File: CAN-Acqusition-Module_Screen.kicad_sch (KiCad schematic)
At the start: 5 parts, among them U9 ERC13232FN-1

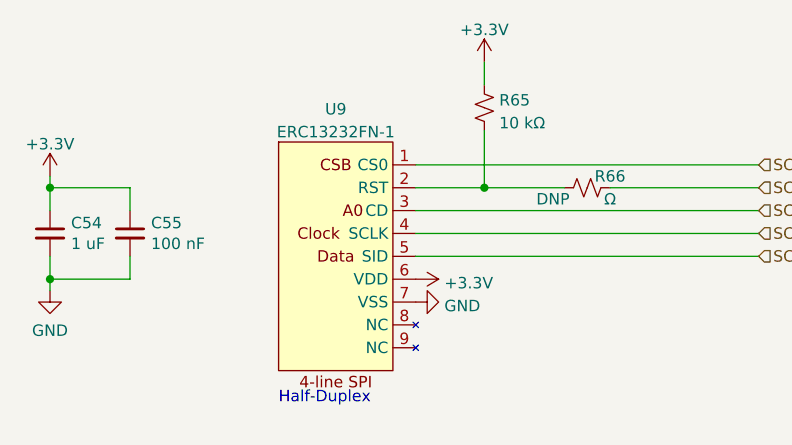
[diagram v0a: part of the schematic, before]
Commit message: Layout of analog section started
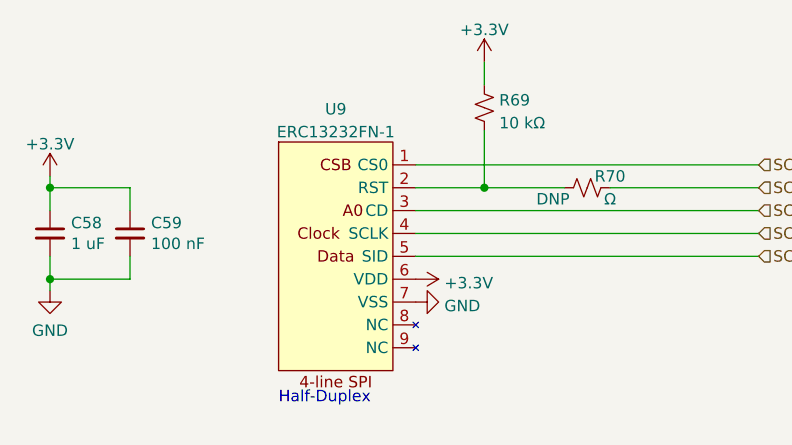
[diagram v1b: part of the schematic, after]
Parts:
- renumbered C54 to C58, C55 to C59, R65 to R69, R66 to R70
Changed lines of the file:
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@@
   (symbol (lib_id "power:+3.3V") (at 144.78 80.01 270) (unit 1)
     (in_bom yes) (on_board yes) (fields_autoplaced)
-    (property "Reference" "#PWR0152" (id 0) (at 140.97 80.01 0)
+    (property "Reference" "#PWR0164" (id 0) (at 140.97 80.01 0)
       (effects (font (size 1.27 1.27)) hide)
     )
@@
   (symbol (lib_id "power:+3.3V") (at 104.14 68.58 0) (unit 1)
     (in_bom yes) (on_board yes) (fields_autoplaced)
-    (property "Reference" "#PWR0150" (id 0) (at 104.14 72.39 0)
+    (property "Reference" "#PWR0162" (id 0) (at 104.14 72.39 0)
       (effects (font (size 1.27 1.27)) hide)
     )
@@
   (symbol (lib_id "Device:C_Small") (at 104.14 74.93 0) (unit 1)
     (in_bom yes) (on_board yes)
-    (property "Reference" "C54" (id 0) (at 106.4768 73.7616 0)
+    (property "Reference" "C58" (id 0) (at 106.4768 73.7616 0)
       (effects (font (size 1.27 1.27)) (justify left))
     )
@@
   (symbol (lib_id "power:GND") (at 144.78 82.55 90) (unit 1)
     (in_bom yes) (on_board yes) (fields_autoplaced)
-    (property "Reference" "#PWR0153" (id 0) (at 151.13 82.55 0)
+    (property "Reference" "#PWR0165" (id 0) (at 151.13 82.55 0)
       (effects (font (size 1.27 1.27)) hide)
     )
@@
   (symbol (lib_id "power:+3.3V") (at 152.4 55.88 0) (unit 1)
     (in_bom yes) (on_board yes) (fields_autoplaced)
-    (property "Reference" "#PWR0154" (id 0) (at 152.4 59.69 0)
+    (property "Reference" "#PWR0166" (id 0) (at 152.4 59.69 0)
       (effects (font (size 1.27 1.27)) hide)
     )
@@
   (symbol (lib_id "Device:C_Small") (at 113.03 74.93 0) (unit 1)
     (in_bom yes) (on_board yes)
-    (property "Reference" "C55" (id 0) (at 115.3668 73.7616 0)
+    (property "Reference" "C59" (id 0) (at 115.3668 73.7616 0)
       (effects (font (size 1.27 1.27)) (justify left))
     )
@@
   (symbol (lib_id "Device:R_Small_US") (at 163.83 69.85 90) (unit 1)
     (in_bom yes) (on_board yes)
-    (property "Reference" "R66" (id 0) (at 166.37 68.58 90))
+    (property "Reference" "R70" (id 0) (at 166.37 68.58 90))
     (property "Value" "Ω" (id 1) (at 166.37 71.12 90))
     (property "Footprint" "Resistor_SMD:R_0603_1608Metric" (id 2) (at 163.83 69.85 0)
@@
   (symbol (lib_id "power:GND") (at 104.14 81.28 0) (unit 1)
     (in_bom yes) (on_board yes) (fields_autoplaced)
-    (property "Reference" "#PWR0151" (id 0) (at 104.14 87.63 0)
+    (property "Reference" "#PWR0163" (id 0) (at 104.14 87.63 0)
       (effects (font (size 1.27 1.27)) hide)
     )
@@
   (symbol (lib_id "Device:R_Small_US") (at 152.4 60.96 0) (unit 1)
     (in_bom yes) (on_board yes) (fields_autoplaced)
-    (property "Reference" "R65" (id 0) (at 154.051 60.1253 0)
+    (property "Reference" "R69" (id 0) (at 154.051 60.1253 0)
       (effects (font (size 1.27 1.27)) (justify left))
     )

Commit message: Finished power outputs
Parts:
- renumbered C58 to C57, C59 to C58, R69 to R70, R70 to R71
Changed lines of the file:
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@@
   (symbol (lib_id "power:+3.3V") (at 144.78 80.01 270) (unit 1)
     (in_bom yes) (on_board yes) (fields_autoplaced)
-    (property "Reference" "#PWR0164" (id 0) (at 140.97 80.01 0)
+    (property "Reference" "#PWR0167" (id 0) (at 140.97 80.01 0)
       (effects (font (size 1.27 1.27)) hide)
     )
@@
   (symbol (lib_id "power:+3.3V") (at 104.14 68.58 0) (unit 1)
     (in_bom yes) (on_board yes) (fields_autoplaced)
-    (property "Reference" "#PWR0162" (id 0) (at 104.14 72.39 0)
+    (property "Reference" "#PWR0165" (id 0) (at 104.14 72.39 0)
       (effects (font (size 1.27 1.27)) hide)
     )
@@
   (symbol (lib_id "Device:C_Small") (at 104.14 74.93 0) (unit 1)
     (in_bom yes) (on_board yes)
-    (property "Reference" "C58" (id 0) (at 106.4768 73.7616 0)
+    (property "Reference" "C57" (id 0) (at 106.4768 73.7616 0)
       (effects (font (size 1.27 1.27)) (justify left))
     )
@@
   (symbol (lib_id "power:GND") (at 144.78 82.55 90) (unit 1)
     (in_bom yes) (on_board yes) (fields_autoplaced)
-    (property "Reference" "#PWR0165" (id 0) (at 151.13 82.55 0)
+    (property "Reference" "#PWR0168" (id 0) (at 151.13 82.55 0)
       (effects (font (size 1.27 1.27)) hide)
     )
@@
   (symbol (lib_id "power:+3.3V") (at 152.4 55.88 0) (unit 1)
     (in_bom yes) (on_board yes) (fields_autoplaced)
-    (property "Reference" "#PWR0166" (id 0) (at 152.4 59.69 0)
+    (property "Reference" "#PWR0169" (id 0) (at 152.4 59.69 0)
       (effects (font (size 1.27 1.27)) hide)
     )
@@
   (symbol (lib_id "Device:C_Small") (at 113.03 74.93 0) (unit 1)
     (in_bom yes) (on_board yes)
-    (property "Reference" "C59" (id 0) (at 115.3668 73.7616 0)
+    (property "Reference" "C58" (id 0) (at 115.3668 73.7616 0)
       (effects (font (size 1.27 1.27)) (justify left))
     )
@@
   (symbol (lib_id "Device:R_Small_US") (at 163.83 69.85 90) (unit 1)
     (in_bom yes) (on_board yes)
-    (property "Reference" "R70" (id 0) (at 166.37 68.58 90))
+    (property "Reference" "R71" (id 0) (at 166.37 68.58 90))
     (property "Value" "Ω" (id 1) (at 166.37 71.12 90))
     (property "Footprint" "Resistor_SMD:R_0603_1608Metric" (id 2) (at 163.83 69.85 0)
@@
   (symbol (lib_id "power:GND") (at 104.14 81.28 0) (unit 1)
     (in_bom yes) (on_board yes) (fields_autoplaced)
-    (property "Reference" "#PWR0163" (id 0) (at 104.14 87.63 0)
+    (property "Reference" "#PWR0166" (id 0) (at 104.14 87.63 0)
       (effects (font (size 1.27 1.27)) hide)
     )
@@
   (symbol (lib_id "Device:R_Small_US") (at 152.4 60.96 0) (unit 1)
     (in_bom yes) (on_board yes) (fields_autoplaced)
-    (property "Reference" "R69" (id 0) (at 154.051 60.1253 0)
+    (property "Reference" "R70" (id 0) (at 154.051 60.1253 0)
       (effects (font (size 1.27 1.27)) (justify left))
     )

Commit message: forgor to save
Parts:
- renumbered C57 to C58, C58 to C59
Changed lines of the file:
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@@
   (symbol (lib_id "power:+3.3V") (at 144.78 80.01 270) (unit 1)
     (in_bom yes) (on_board yes) (fields_autoplaced)
-    (property "Reference" "#PWR0167" (id 0) (at 140.97 80.01 0)
+    (property "Reference" "#PWR0168" (id 0) (at 140.97 80.01 0)
       (effects (font (size 1.27 1.27)) hide)
     )
@@
   (symbol (lib_id "power:+3.3V") (at 104.14 68.58 0) (unit 1)
     (in_bom yes) (on_board yes) (fields_autoplaced)
-    (property "Reference" "#PWR0165" (id 0) (at 104.14 72.39 0)
+    (property "Reference" "#PWR0166" (id 0) (at 104.14 72.39 0)
       (effects (font (size 1.27 1.27)) hide)
     )
@@
   (symbol (lib_id "Device:C_Small") (at 104.14 74.93 0) (unit 1)
     (in_bom yes) (on_board yes)
-    (property "Reference" "C57" (id 0) (at 106.4768 73.7616 0)
+    (property "Reference" "C58" (id 0) (at 106.4768 73.7616 0)
       (effects (font (size 1.27 1.27)) (justify left))
     )
@@
   (symbol (lib_id "power:GND") (at 144.78 82.55 90) (unit 1)
     (in_bom yes) (on_board yes) (fields_autoplaced)
-    (property "Reference" "#PWR0168" (id 0) (at 151.13 82.55 0)
+    (property "Reference" "#PWR0169" (id 0) (at 151.13 82.55 0)
       (effects (font (size 1.27 1.27)) hide)
     )
@@
   (symbol (lib_id "power:+3.3V") (at 152.4 55.88 0) (unit 1)
     (in_bom yes) (on_board yes) (fields_autoplaced)
-    (property "Reference" "#PWR0169" (id 0) (at 152.4 59.69 0)
+    (property "Reference" "#PWR0170" (id 0) (at 152.4 59.69 0)
       (effects (font (size 1.27 1.27)) hide)
     )
@@
   (symbol (lib_id "Device:C_Small") (at 113.03 74.93 0) (unit 1)
     (in_bom yes) (on_board yes)
-    (property "Reference" "C58" (id 0) (at 115.3668 73.7616 0)
+    (property "Reference" "C59" (id 0) (at 115.3668 73.7616 0)
       (effects (font (size 1.27 1.27)) (justify left))
     )
@@
   (symbol (lib_id "power:GND") (at 104.14 81.28 0) (unit 1)
     (in_bom yes) (on_board yes) (fields_autoplaced)
-    (property "Reference" "#PWR0166" (id 0) (at 104.14 87.63 0)
+    (property "Reference" "#PWR0167" (id 0) (at 104.14 87.63 0)
       (effects (font (size 1.27 1.27)) hide)
     )

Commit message: Rev. A1 release
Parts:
- renumbered C58 to C59, C59 to C60, R70 to R72, R71 to R73, U9 to U10
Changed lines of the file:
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@@
   (symbol (lib_id "power:+3.3V") (at 144.78 80.01 270) (unit 1)
     (in_bom yes) (on_board yes) (fields_autoplaced)
-    (property "Reference" "#PWR0168" (id 0) (at 140.97 80.01 0)
+    (property "Reference" "#PWR0172" (id 0) (at 140.97 80.01 0)
       (effects (font (size 1.27 1.27)) hide)
     )
@@
   (symbol (lib_id "power:+3.3V") (at 104.14 68.58 0) (unit 1)
     (in_bom yes) (on_board yes) (fields_autoplaced)
-    (property "Reference" "#PWR0166" (id 0) (at 104.14 72.39 0)
+    (property "Reference" "#PWR0170" (id 0) (at 104.14 72.39 0)
       (effects (font (size 1.27 1.27)) hide)
     )
@@
   (symbol (lib_id "Device:C_Small") (at 104.14 74.93 0) (unit 1)
     (in_bom yes) (on_board yes)
-    (property "Reference" "C58" (id 0) (at 106.4768 73.7616 0)
+    (property "Reference" "C59" (id 0) (at 106.4768 73.7616 0)
       (effects (font (size 1.27 1.27)) (justify left))
     )
@@
   (symbol (lib_id "power:GND") (at 144.78 82.55 90) (unit 1)
     (in_bom yes) (on_board yes) (fields_autoplaced)
-    (property "Reference" "#PWR0169" (id 0) (at 151.13 82.55 0)
+    (property "Reference" "#PWR0173" (id 0) (at 151.13 82.55 0)
       (effects (font (size 1.27 1.27)) hide)
     )
@@
   (symbol (lib_id "power:+3.3V") (at 152.4 55.88 0) (unit 1)
     (in_bom yes) (on_board yes) (fields_autoplaced)
-    (property "Reference" "#PWR0170" (id 0) (at 152.4 59.69 0)
+    (property "Reference" "#PWR0174" (id 0) (at 152.4 59.69 0)
       (effects (font (size 1.27 1.27)) hide)
     )
@@
   (symbol (lib_id "Device:C_Small") (at 113.03 74.93 0) (unit 1)
     (in_bom yes) (on_board yes)
-    (property "Reference" "C59" (id 0) (at 115.3668 73.7616 0)
+    (property "Reference" "C60" (id 0) (at 115.3668 73.7616 0)
       (effects (font (size 1.27 1.27)) (justify left))
     )
@@
   (symbol (lib_id "Device:R_Small_US") (at 163.83 69.85 90) (unit 1)
     (in_bom yes) (on_board yes)
-    (property "Reference" "R71" (id 0) (at 166.37 68.58 90))
+    (property "Reference" "R73" (id 0) (at 166.37 68.58 90))
     (property "Value" "Ω" (id 1) (at 166.37 71.12 90))
     (property "Footprint" "Resistor_SMD:R_0603_1608Metric" (id 2) (at 163.83 69.85 0)
@@
   (symbol (lib_id "power:GND") (at 104.14 81.28 0) (unit 1)
     (in_bom yes) (on_board yes) (fields_autoplaced)
-    (property "Reference" "#PWR0167" (id 0) (at 104.14 87.63 0)
+    (property "Reference" "#PWR0171" (id 0) (at 104.14 87.63 0)
       (effects (font (size 1.27 1.27)) hide)
     )
@@
   (symbol (lib_id "Device:R_Small_US") (at 152.4 60.96 0) (unit 1)
     (in_bom yes) (on_board yes) (fields_autoplaced)
-    (property "Reference" "R70" (id 0) (at 154.051 60.1253 0)
+    (property "Reference" "R72" (id 0) (at 154.051 60.1253 0)
       (effects (font (size 1.27 1.27)) (justify left))
     )
@@
   (symbol (lib_id "CAN-Acquisition-Module:ERC13232FN-1") (at 129.54 64.77 0) (unit 1)
     (in_bom yes) (on_board yes) (fields_autoplaced)
-    (property "Reference" "U9" (id 0) (at 135.89 61.121 0))
+    (property "Reference" "U10" (id 0) (at 135.89 61.121 0))
     (property "Value" "ERC13232FN-1" (id 1) (at 135.89 63.6579 0))
     (property "Footprint" "CAN-Acquisition-Module:ERC13232FN-1" (id 2) (at 138.43 99.06 0)

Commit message: Added as-ordered P/Ns and regenerated Gerbers
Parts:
- R72: Mfr. (none) -> Stackpole; P/N (none) -> RMCF0603FT10K0
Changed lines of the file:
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@@
+      (effects (font (size 1.27 1.27)) hide)
+    )
+    (property "Mfr." "Stackpole" (id 4) (at 152.4 60.96 0)
+      (effects (font (size 1.27 1.27)) hide)
+    )
+    (property "P/N" "RMCF0603FT10K0" (id 5) (at 152.4 60.96 0)
       (effects (font (size 1.27 1.27)) hide)
     )

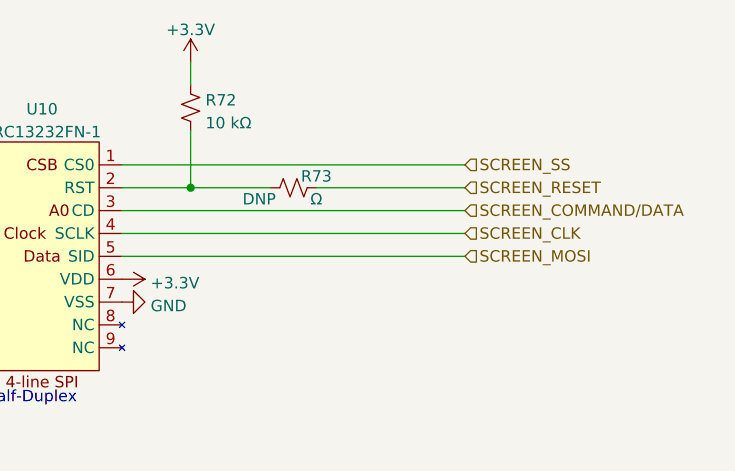
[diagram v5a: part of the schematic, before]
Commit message: Rev.A2 pretty much finished
V USB bypasses inductor L2
Srew terminal pin holes size reduced
Thermally isolated SHT3x
Fixed U1 footprint
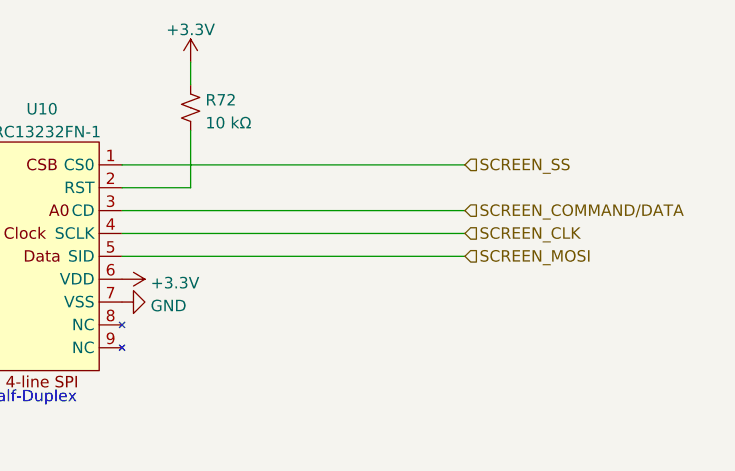
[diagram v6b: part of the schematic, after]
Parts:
- removed R73: Ω, Resistor_SMD:R_0603_1608Metric, symbol Device:R_Small_US
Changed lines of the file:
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@@
   (junction (at 104.14 80.01) (diameter 0) (color 0 0 0 0)
-  )
-  (junction (at 152.4 69.85) (diameter 0) (color 0 0 0 0)
   )
   (wire (pts (xy 104.14 80.01) (xy 104.14 77.47))
@@
     (stroke (width 0) (type default) (color 0 0 0 0))
   )
-  (wire (pts (xy 166.37 69.85) (xy 182.88 69.85))
-    (stroke (width 0) (type default) (color 0 0 0 0))
-  )
   (wire (pts (xy 144.78 77.47) (xy 182.88 77.47))
     (stroke (width 0) (type default) (color 0 0 0 0))
   )
   (wire (pts (xy 113.03 80.01) (xy 113.03 77.47))
-    (stroke (width 0) (type default) (color 0 0 0 0))
-  )
-  (wire (pts (xy 152.4 69.85) (xy 161.29 69.85))
     (stroke (width 0) (type default) (color 0 0 0 0))
   )
@@
   )
   (hierarchical_label "SCREEN_MOSI" (shape input) (at 182.88 77.47 0)
-    (effects (font (size 1.27 1.27)) (justify left))
-  )
-  (hierarchical_label "SCREEN_RESET" (shape input) (at 182.88 69.85 0)
     (effects (font (size 1.27 1.27)) (justify left))
   )
@@
     (pin "1")
     (pin "2")
-  )
-  (symbol (lib_id "Device:R_Small_US") (at 163.83 69.85 90) (unit 1)
-    (in_bom yes) (on_board yes)
-    (property "Reference" "R73" (id 0) (at 166.37 68.58 90))
-    (property "Value" "Ω" (id 1) (at 166.37 71.12 90))
-    (property "Footprint" "Resistor_SMD:R_0603_1608Metric" (id 2) (at 163.83 69.85 0)
-      (effects (font (size 1.27 1.27)) hide)
-    )
-    (property "Datasheet" "~" (id 3) (at 163.83 69.85 0)
-      (effects (font (size 1.27 1.27)) hide)
-    )
-    (property "Do Not Place" "DNP" (id 4) (at 160.02 71.12 90))
-    (pin "1")
-    (pin "2")

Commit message: Fixed board and re-exported Gerbers. BOM is a WIP
Some design rules were violated
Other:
- company: (none) -> École de Technologie Supérieure - Laboratoire thermique et science du bâtiment (LTSB)
- title: (none) -> CANbus Acquisition Module
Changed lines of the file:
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@@
 (kicad_sch (version 20211123) (generator eeschema)
   (paper "A4")
+  (title_block
+    (title "CANbus Acquisition Module")
+    (date "2022-10-04")
+    (rev "A3")
+    (company "École de Technologie Supérieure - Laboratoire thermique et science du bâtiment (LTSB)")
+    (comment 1 "Designer: Hugo Boyce")
+  )
   (junction (at 104.14 69.85) (diameter 0) (color 0 0 0 0)
   )

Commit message: BOM updated for LCSC. Still a WIP.
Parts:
- R72: Tolerance (none) -> 1%
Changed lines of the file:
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@@
+      (effects (font (size 1.27 1.27)) hide)
+    )
+    (property "Tolerance" "1%" (id 6) (at 152.4 60.96 0)
       (effects (font (size 1.27 1.27)) hide)
     )
